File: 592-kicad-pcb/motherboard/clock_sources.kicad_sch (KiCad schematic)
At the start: 0 parts

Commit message: add schematic for clock generator, some symbols
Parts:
- added C1, C2, C3, C4: 0.1u, symbol Device:C_Small
- added C5, C6: 2p, symbol Device:C_Small
- added J1: Conn_Coaxial_Small, symbol Connector:Conn_Coaxial_Small
- added R1, R2: 10k, symbol Device:R_Small
- added R3, R4, R5: 0, symbol Device:R_Small
- added U1, U3: SN74LVC1G3157DBVR, symbol 592-partslib:SN74LVC1G3157DBVR
- added U2: SMXS-04K, symbol 592-partslib:SMXS-04K
- added Y1: Si5351A-B-GT, Package_SO:MSOP-10_3x3mm_P0.5mm, symbol Oscillator:Si5351A-B-GT
- added Y2: 25M, symbol Device:Crystal_GND24_Small
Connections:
- new net: R3.1, Y1.10 (CLK0)
- new net: Y1.2 (XA), Y2.3
- new net: Y1.3 (XB), Y2.1
- new net: R5.1, Y1.6 (CLK2)
- new net: R4.1, Y1.9 (CLK1)
- new net: C5.1, Y2.2
- new net: C6.1, Y2.4
- new net +1V8: C2.1, Y1.7 (VDDO)
- new net +3V3: C1.1, R1.1, R2.1, U1.5 (VCC), U3.5 (VCC), Y1.1 (VDD)
- new net CLOCK_UNCORE: R5.2
- new net EXT_CLK_DIG: U3.4 (A)
- new net EXT_CLK_DIG_AUX: J1.1 (In), U3.3 (B1)
- new net EXT_CLK_DIG_GEN: R4.2, U3.1 (B2)
- new net EXT_CLK_DIG_SEL: C3.2, R2.2, U2.7 (2o), U3.6 (S)
- new net FS_EXT: U1.4 (A)
- new net FS_EXT_AUX: U1.3 (B1)
- new net FS_EXT_GEN: R3.2, U1.1 (B2)
- new net FS_EXT_SEL: C4.2, R1.2, U1.6 (S), U2.8 (1o)
- new net GND: C1.2, C2.2, C3.1, C4.1, C5.2, C6.2, J1.2 (Ext), U1.2 (GND), U2.1 (1i), U2.2 (2i), U3.2 (GND), Y1.8 (GND)
- new net SCL: Y1.4 (SCL)
- new net SDA: Y1.5 (SDA)
- no-connect marks 0 -> 4
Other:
- note added: "assume GPIO connects to *SEL pins in open-drain config to drive PDN to ground to change setting"
- note added: "caps selected for 1khz bw reject switch bounce"
- note added: "control lines to 50 ohm as applicable"
- note added: "resistors for EMI (optional)"
- note added: "sequence vddo to come on at or before vdd"
- company: (none) -> john kesler (jckesle2@ncsu.edu)
- title: (none) -> clock source generators

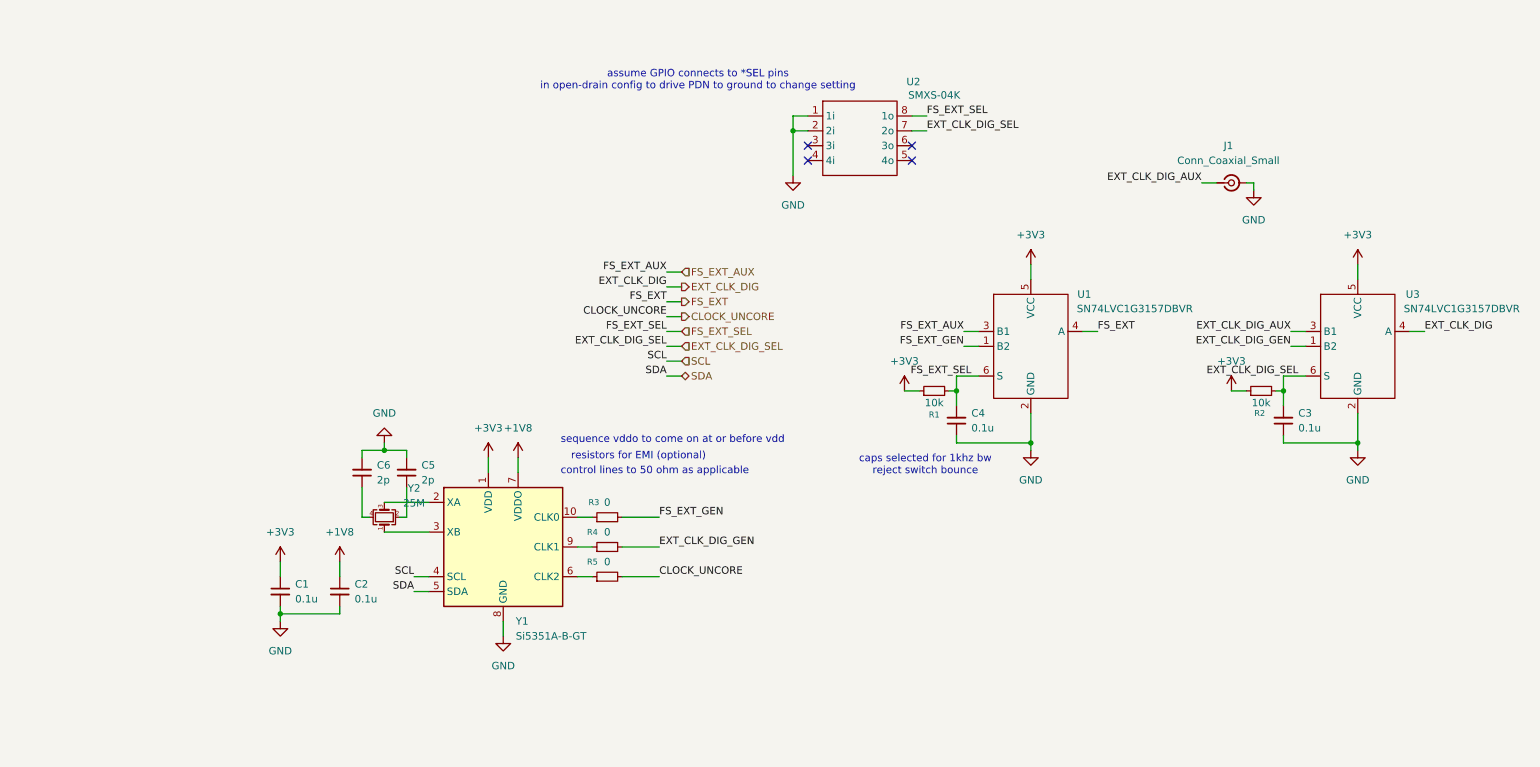
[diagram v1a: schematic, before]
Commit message: update signal supporting ckts
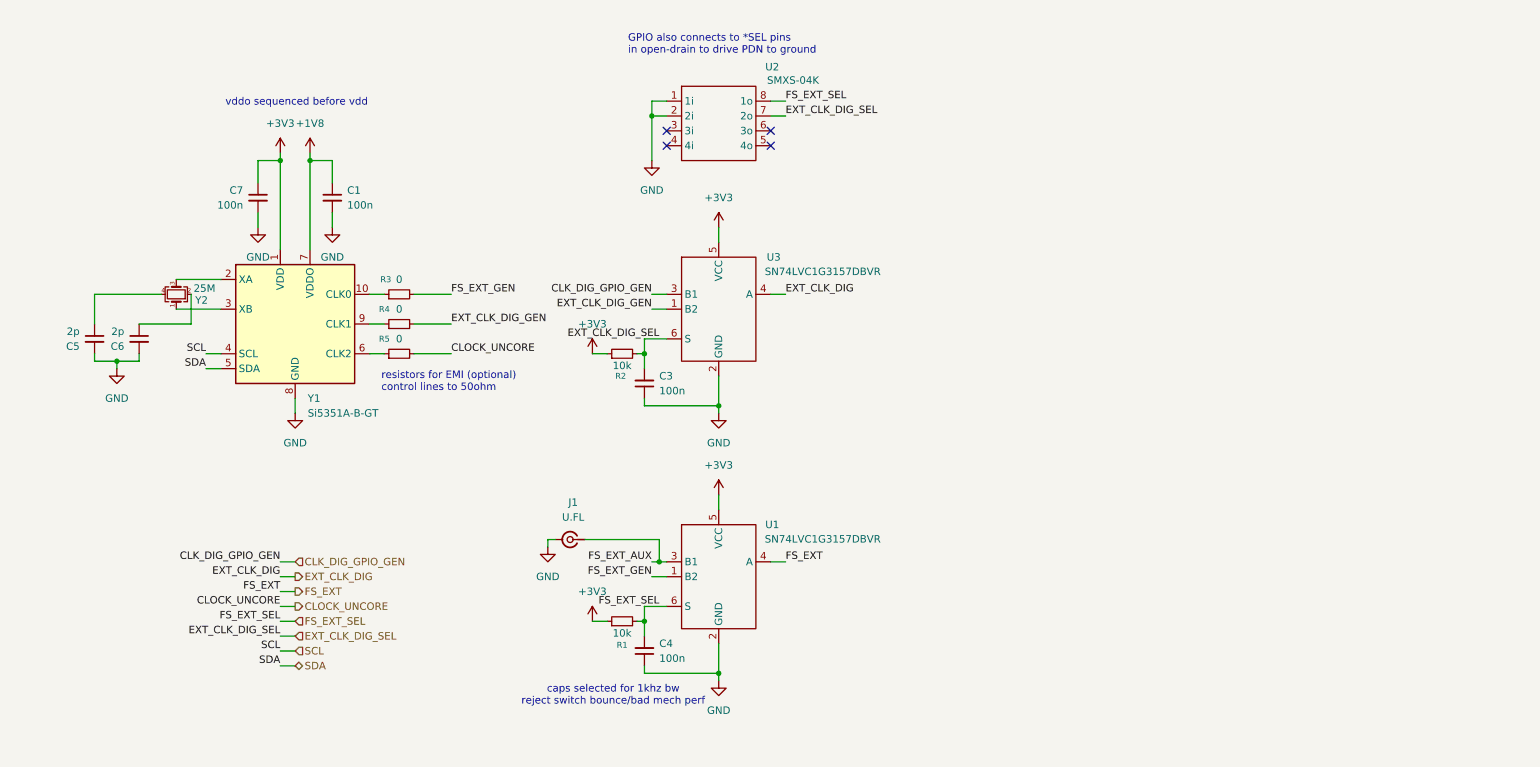
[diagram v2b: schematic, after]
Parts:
- removed C2: 0.1u, symbol Device:C_Small
- added C7: 100n, symbol Device:C_Small
- C1, C3, C4: value 0.1u -> 100n
- J1: value Conn_Coaxial_Small -> U.FL
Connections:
- net +1V8: now also C1.1
- net +3V3: now also C7.1; no longer C1.1
- net FS_EXT_AUX: now also J1.1 (In)
- net GND: now also C7.2
- net at Y2.2: now also C6.1; no longer C5.1
- net at Y2.4: now also C5.1; no longer C6.1
- net EXT_CLK_DIG_AUX renamed CLK_DIG_GPIO_GEN
- net CLK_DIG_GPIO_GEN: no longer J1.1 (In)
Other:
- note added: "GPIO also connects to *SEL pins in open-drain to drive PDN to ground"
- note added: "caps selected for 1khz bw reject switch bounce/bad mech perf"
- note added: "resistors for EMI (optional) control lines to 50ohm"
- note added: "vddo sequenced before vdd"
- note removed: "assume GPIO connects to *SEL pins in open-drain config to drive PDN to ground to change setting"
- note removed: "caps selected for 1khz bw reject switch bounce"
- note removed: "control lines to 50 ohm as applicable"
- note removed: "resistors for EMI (optional)"
- note removed: "sequence vddo to come on at or before vdd"
- moved on the sheet: C1, C3, C4, C5, C6, J1, R1, R2, R3, R4, R5, U1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

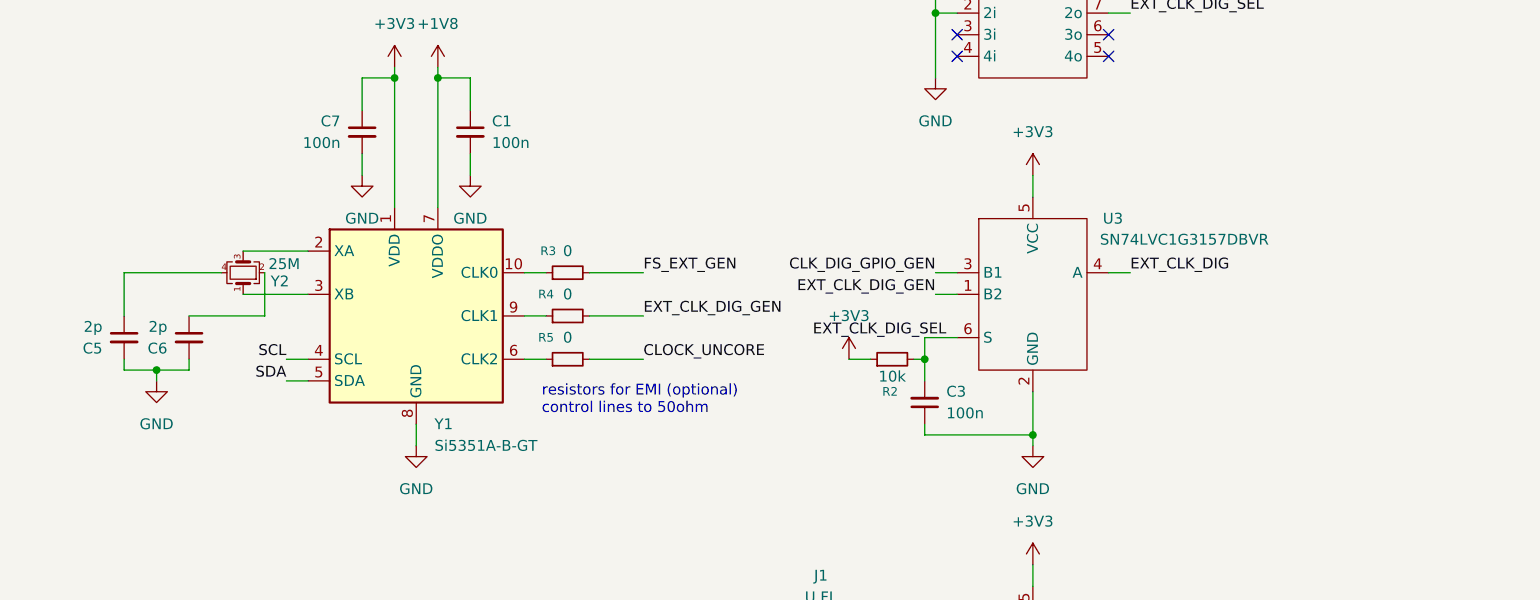
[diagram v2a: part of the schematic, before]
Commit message: clean up supporting blocks; add nucleo symbol
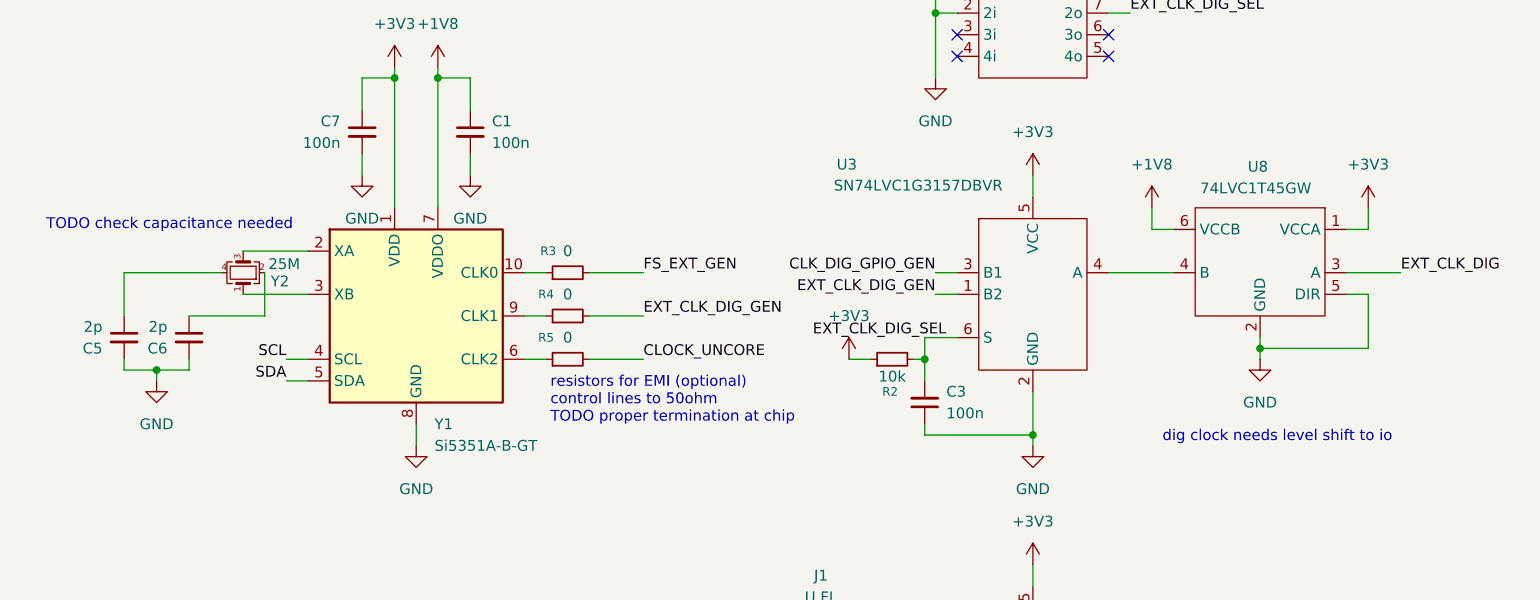
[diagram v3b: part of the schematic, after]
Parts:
- added U8: 74LVC1T45GW, symbol 592-partslib:74LVC1T45GW
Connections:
- net +1V8: now also U8.6 (VCCB)
- net +3V3: now also U8.1 (VCCA)
- net EXT_CLK_DIG: now also U8.3 (A); no longer U3.4 (A)
- net GND: now also U8.2 (GND), U8.5 (DIR)
- new net: U3.4 (A), U8.4 (B)
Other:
- note added: "TODO check capacitance needed"
- note added: "dig clock needs level shift to io"
- note added: "resistors for EMI (optional) control lines to 50ohm TODO proper termination at chip"
- note removed: "resistors for EMI (optional) control lines to 50ohm"

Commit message: add footprints for signal conditioning
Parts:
- C1, C3, C4, C5, C6, C7, R1, R2, R3, R4, R5: footprint (none) -> Capacitor_SMD:C_0603_1608Metric
- J1: footprint (none) -> Connector_Coaxial:U.FL_Hirose_U.FL-R-SMT-1_Vertical
- U1, U3: footprint (none) -> Package_TO_SOT_SMD:SOT-23-6
- U2: footprint (none) -> 592-partslib:SMXS-04K-TP
- U8: footprint (none) -> Package_TO_SOT_SMD:SOT-363_SC-70-6
- Y2: footprint (none) -> Crystal:Crystal_SMD_3225-4Pin_3.2x2.5mm
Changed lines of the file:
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@@
 			)
 		)
-		(property "Footprint" ""
+		(property "Footprint" "Crystal:Crystal_SMD_3225-4Pin_3.2x2.5mm"
 			(at 41.91 66.04 0)
 			(effects
@@
 			)
 		)
-		(property "Footprint" ""
+		(property "Footprint" "Capacitor_SMD:C_0603_1608Metric"
 			(at 118.11 121.92 0)
 			(effects
@@
 			)
 		)
-		(property "Footprint" ""
+		(property "Footprint" "Capacitor_SMD:C_0603_1608Metric"
 			(at 27.94 73.66 0)
 			(effects
@@
 			)
 		)
-		(property "Footprint" ""
+		(property "Footprint" "Capacitor_SMD:C_0603_1608Metric"
 			(at 80.01 76.2 0)
 			(effects
@@
 			)
 		)
-		(property "Footprint" ""
+		(property "Footprint" "Capacitor_SMD:C_0603_1608Metric"
 			(at 80.01 66.04 0)
 			(effects
@@
 			)
 		)
-		(property "Footprint" ""
+		(property "Footprint" "Capacitor_SMD:C_0603_1608Metric"
 			(at 121.92 127 0)
 			(effects
@@
 			)
 		)
-		(property "Footprint" ""
+		(property "Footprint" "592-partslib:SMXS-04K-TP"
 			(at 134.62 36.83 0)
 			(effects
@@
 			)
 		)
-		(property "Footprint" ""
+		(property "Footprint" "Connector_Coaxial:U.FL_Hirose_U.FL-R-SMT-1_Vertical"
 			(at 109.22 107.95 0)
 			(effects
@@
 			)
 		)
-		(property "Footprint" ""
+		(property "Footprint" "Package_TO_SOT_SMD:SOT-363_SC-70-6"
 			(at 161.29 64.77 0)
 			(effects
@@
 			)
 		)
-		(property "Footprint" ""
+		(property "Footprint" "Package_TO_SOT_SMD:SOT-23-6"
 			(at 115.57 109.22 0)
 			(effects
@@
 			)
 		)
-		(property "Footprint" ""
+		(property "Footprint" "Capacitor_SMD:C_0603_1608Metric"
 			(at 118.11 76.2 0)
 			(effects
@@
 			)
 		)
-		(property "Footprint" ""
+		(property "Footprint" "Capacitor_SMD:C_0603_1608Metric"
 			(at 55.88 49.53 0)
 			(effects
@@
 			)
 		)
-		(property "Footprint" ""
+		(property "Footprint" "Capacitor_SMD:C_0603_1608Metric"
 			(at 68.58 49.53 0)
 			(effects
@@
 			)
 		)
-		(property "Footprint" ""
+		(property "Footprint" "Package_TO_SOT_SMD:SOT-23-6"
 			(at 115.57 63.5 0)
 			(effects
@@
 			)
 		)
-		(property "Footprint" ""
+		(property "Footprint" "Capacitor_SMD:C_0603_1608Metric"
 			(at 80.01 71.12 0)
 			(effects
@@
 			)
 		)
-		(property "Footprint" ""
+		(property "Footprint" "Capacitor_SMD:C_0603_1608Metric"
 			(at 35.56 73.66 0)
 			(effects
@@
 			)
 		)
-		(property "Footprint" ""
+		(property "Footprint" "Capacitor_SMD:C_0603_1608Metric"
 			(at 121.92 81.28 0)
 			(effects

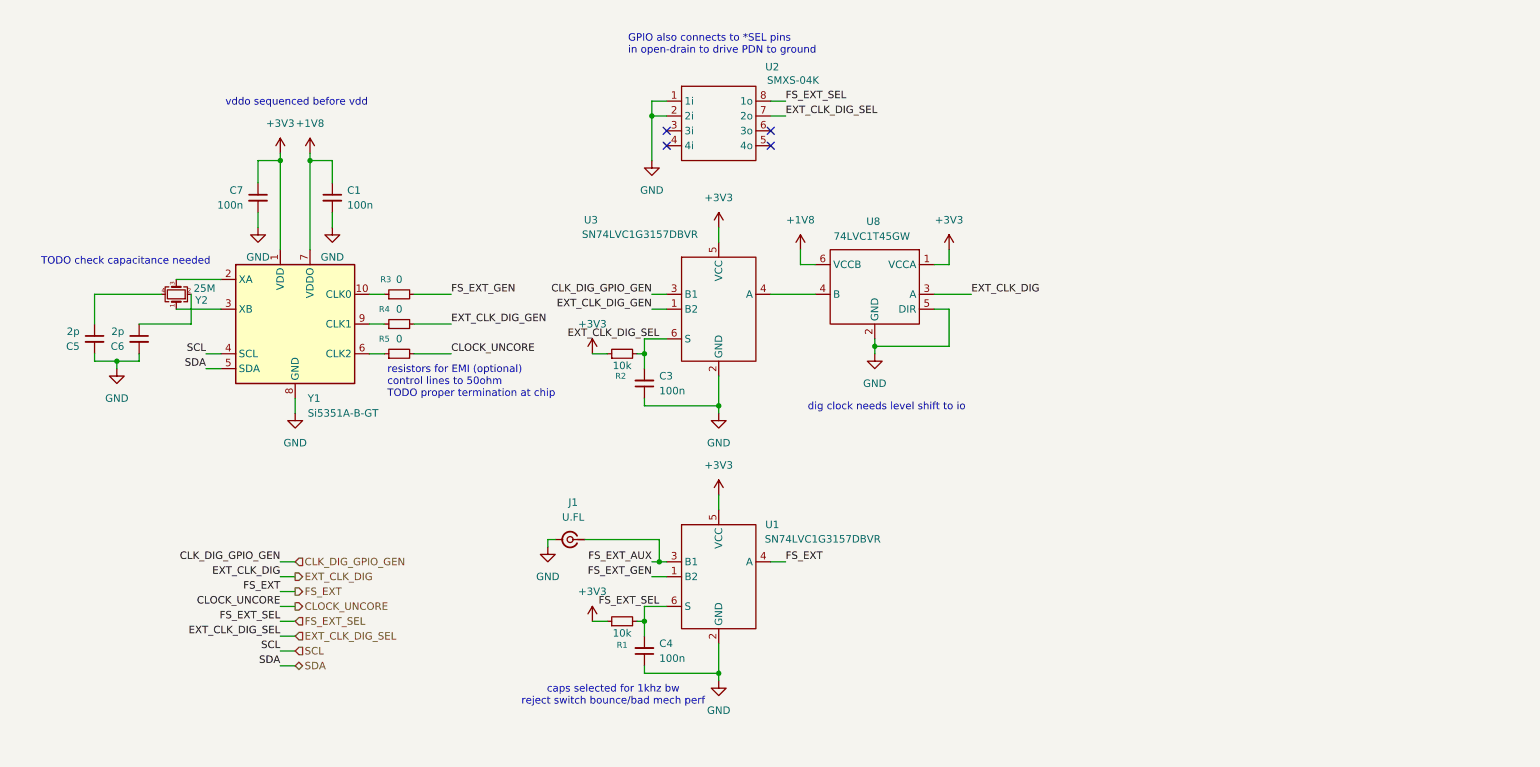
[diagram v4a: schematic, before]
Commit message: update motheboard schems to include conn
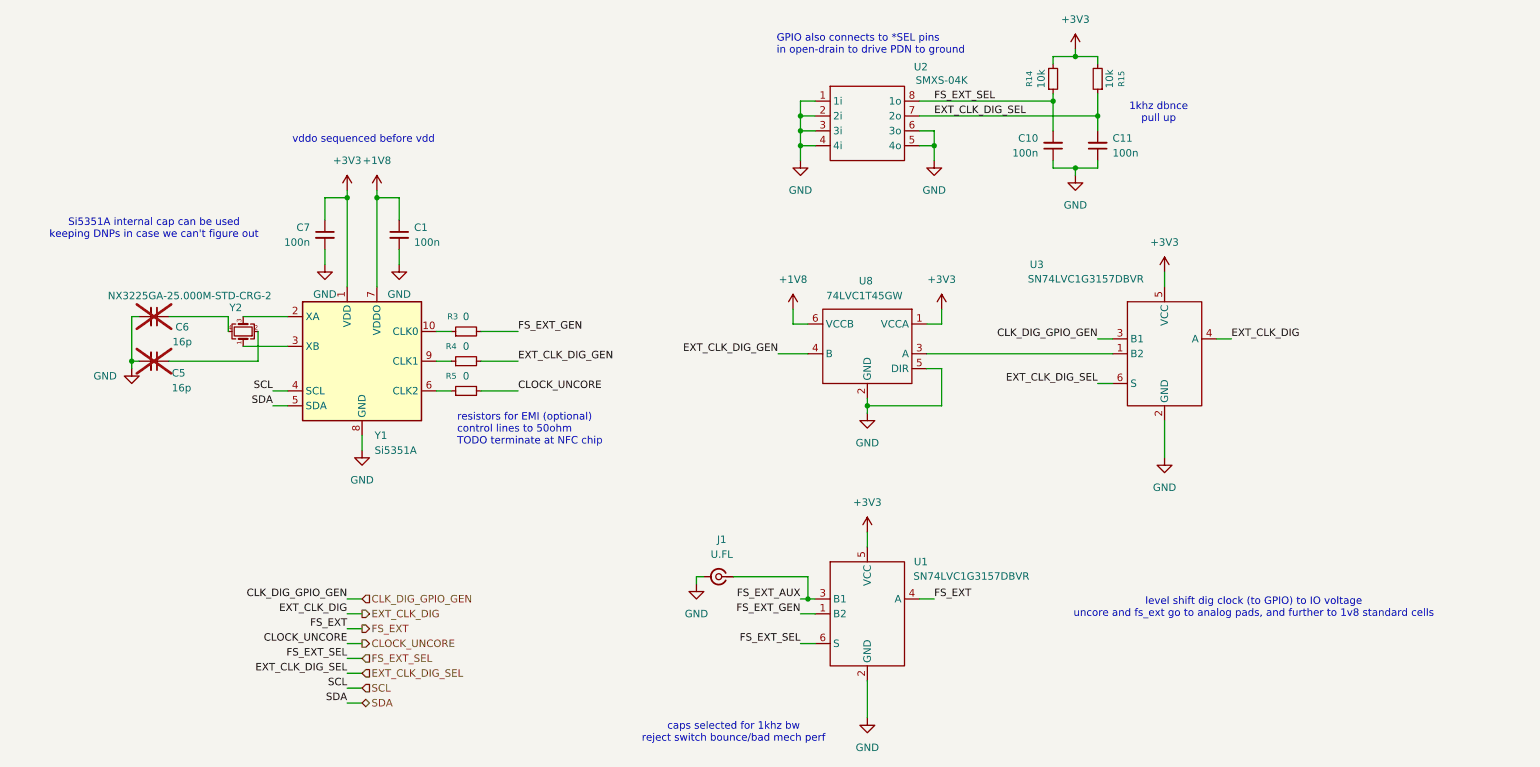
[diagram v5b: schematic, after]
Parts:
- removed C3, C4: 100n, Capacitor_SMD:C_0603_1608Metric, symbol Device:C_Small
- removed R1, R2: 10k, Capacitor_SMD:C_0603_1608Metric, symbol Device:R_Small
- added C10, C11: 100n, Capacitor_SMD:C_0603_1608Metric, symbol Device:C_Small
- added R14, R15: 10k, Capacitor_SMD:C_0603_1608Metric, symbol Device:R_Small
- C5, C6: value 2p -> 16p; now not fitted
- Y1: value Si5351A-B-GT -> Si5351A
- Y2: value 25M -> NX3225GA-25.000M-STD-CRG-2
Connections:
- net +3V3: now also R14.2, R15.2
- net EXT_CLK_DIG: now also U3.4 (A); no longer U8.3 (A)
- net EXT_CLK_DIG_GEN: now also U8.4 (B); no longer U3.1 (B2)
- net EXT_CLK_DIG_SEL: now also C11.2, R15.1
- net FS_EXT_SEL: now also C10.2, R14.1
- net GND: now also U2.3 (3i), U2.4 (4i), U2.5 (4o), U2.6 (3o), C10.1, C11.1
- net at Y2.2: now also C5.1; no longer C6.1
- net at Y2.4: now also C6.1; no longer C5.1
- new net: U3.1 (B2), U8.3 (A)
- no-connect marks 4 -> 0
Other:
- note added: "1khz dbnce pull up"
- note added: "Si5351A internal cap can be used keeping DNPs in case we can't figure out"
- note added: "level shift dig clock (to GPIO) to IO voltage uncore and fs_ext go to analog pads, and further to 1v8 standard cells"
- note added: "resistors for EMI (optional) control lines to 50ohm TODO terminate at NFC chip"
- note removed: "TODO check capacitance needed"
- note removed: "dig clock needs level shift to io"
- note removed: "resistors for EMI (optional) control lines to 50ohm TODO proper termination at chip"
- moved on the sheet: C1, C7, J1, R3, R4, R5, U1, U2, U3, U8, Y1, Y2
